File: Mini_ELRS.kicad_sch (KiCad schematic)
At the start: 30 parts, among them J1 Conn_01x02, J2 Conn_01x03_MountingPin, J3 Conn_01x04, J4 Conn_01x03_MountingPin, J5 Conn_01x03_MountingPin, J6 Conn_01x03_MountingPin, Q1 Q_NMOS_GSD, Q2 Q_NMOS_GSD, U1 ESP32-PICO-D4, U2 TC2014-3.3VxCTTR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

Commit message: finished TX mobile
Signed-off-by: huangzzk <huangcmzzk@gmail.com>
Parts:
- removed C3: 180pF, Capacitor_SMD:C_0603_1608Metric, symbol Device:C
- removed J1: Conn_01x02, Connector_PinHeader_2.54mm:PinHeader_2x01_P2.54mm_Vertical, symbol Connector_Generic:Conn_01x02
- removed J2, J4, J5, J6: Conn_01x03_MountingPin, Connector_Molex:Molex_CLIK-Mate_502386-0370_1x03-1MP_P1.25mm_Horizontal, symbol Connector_Generic_MountingPin:Conn_01x03_MountingPin
- removed R2: NC, Resistor_SMD:R_0603_1608Metric, symbol Device:R
- added R7: 10K, Resistor_SMD:R_0603_1608Metric, symbol Device:R
- added TP1: TestPoint, TestPoint:TestPoint_Pad_1.0x1.0mm, symbol Connector:TestPoint
- added U4: CH340E, Package_SO:MSOP-10_3x3mm_P0.5mm, symbol Interface_USB:CH340E
- added USB1: 918-118A2021Y40002, ic_footprint:TYPE-C-SMD_JINGTUOJIN_918-118A2021Y40002, symbol ic:918-118A2021Y40002
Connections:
- net PWM6 is gone; now on net MOSI: U1.36 (IO23)
- net PWM8 is gone; now on net BUSY: U1.42 (IO21)
- net +3V3: now also R7.2, U4.10 (V3), U4.7 (VCC)
- net BUSY: no longer U1.5 (SENSOR_VP)
- net DIO1: now also U1.24 (IO4); no longer U1.7 (SENSOR_CAPN)
- net GND: now also R4.1, U4.3 (GND), USB1.1 (G), USB1.16 (G), USB1.17, USB1.18, USB1.8 (G), USB1.9 (G); no longer R4.2, R6.2
- net LED: now also U1.21 (IO15); no longer U1.22 (IO2)
- net MISO: now also U1.38 (IO19); no longer U1.8 (SENSOR_VN)
- net MOSI: no longer U1.16 (IO27)
- net NRST: now also U1.17 (IO14); no longer U1.24 (IO4)
- net NSS: now also U1.34 (IO5); no longer R6.1, U1.20 (IO13)
- net SCK: now also U1.35 (IO18); no longer U1.18 (IO12)
- net at Q1.3 (D): now also Q2.1 (G), R6.1
- net CRSF: now reaches Q2.3 (D)
- net CRSF: now also U1.20 (IO13), R7.1, U4.9 (RXD)
- net at U1.23 (IO0): now also TP1.1
- net +BATT renamed +5V
- net +5V: now also USB1.10 (V), USB1.15 (V), USB1.2 (V), USB1.7 (V)
- net PWM1: no longer names the net of U1.28 (SD2/IO9)
- net PWM2: no longer names the net of U1.14 (IO25)
- removed net PWM3: Q2.1 (G), R5.1, U1.34 (IO5)
- net PWM4: no longer names the net of U1.13 (IO33)
- removed net PWM5: Q1.1 (G), R4.1, U1.39 (IO22)
- net PWM7: no longer names the net of U1.12 (IO32)
- new net: R5.1, USB1.11 (CC2)
- new net: R4.2, USB1.6 (CC1)
- new net CRSF_TX: Q1.1 (G), U4.8 (TXD)
- new net DN: U4.2 (UD-), USB1.13 (D-), USB1.4 (D-)
- new net DP: U4.1 (UD+), USB1.12 (D+), USB1.5 (D+)
- new net TNOW: R6.2, U4.6 (TNOW)
- no-connect marks 3 -> 4
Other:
- moved on the sheet: C2, C4, U2

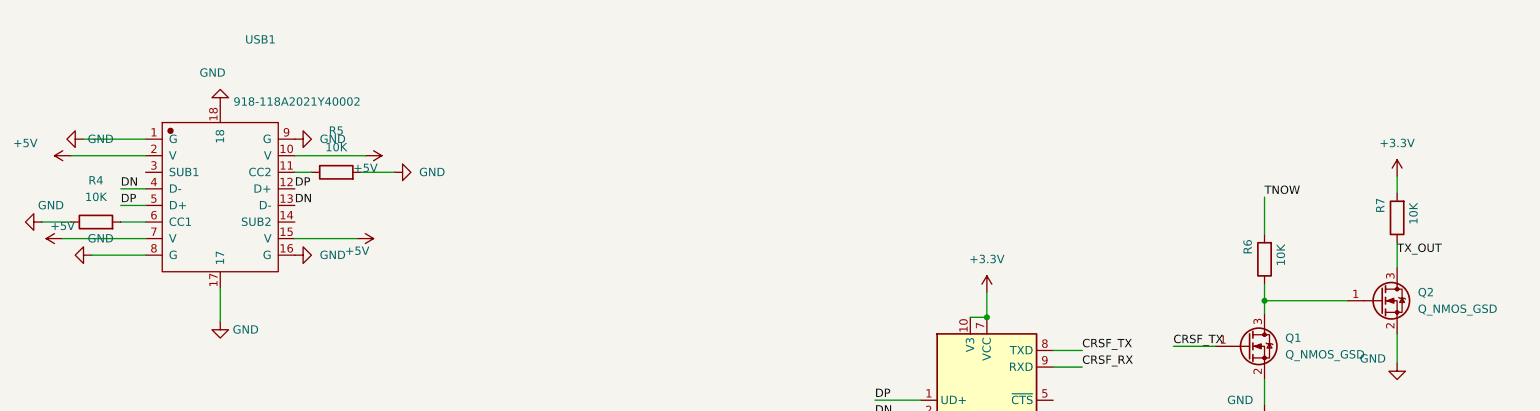
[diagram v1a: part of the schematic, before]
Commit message: change some value of res
Signed-off-by: huangzzk <huangcmzzk@gmail.com>
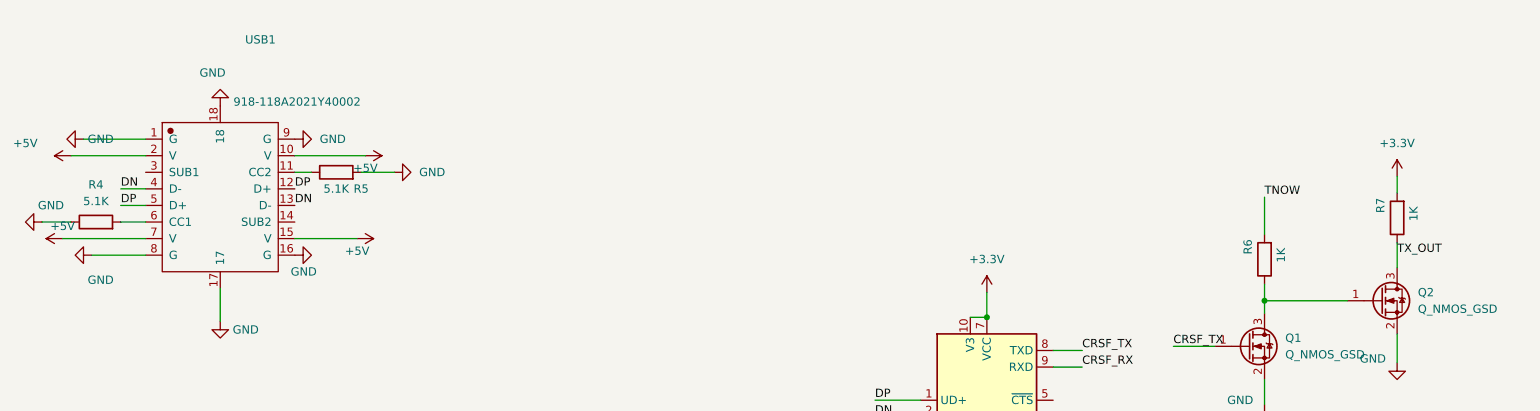
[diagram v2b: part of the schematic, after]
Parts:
- R4, R5: value 10K -> 5.1K
- R6, R7: value 10K -> 1K
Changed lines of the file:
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@@
   )
   (symbol (lib_id "power:GND") (at 72.39 213.995 90) (unit 1)
-    (in_bom yes) (on_board yes) (fields_autoplaced)
+    (in_bom yes) (on_board yes)
     (property "Reference" "#PWR010" (id 0) (at 78.74 213.995 0)
       (effects (font (size 1.27 1.27)) hide)
     )
-    (property "Value" "GND" (id 1) (at 76.2 213.9949 90)
+    (property "Value" "GND" (id 1) (at 71.755 216.535 90)
       (effects (font (size 1.27 1.27)) (justify right))
     )
@@
     (in_bom yes) (on_board yes)
     (property "Reference" "R7" (id 0) (at 238.76 206.375 90))
-    (property "Value" "10K" (id 1) (at 243.84 207.645 90))
+    (property "Value" "1K" (id 1) (at 243.84 207.645 90))
     (property "Footprint" "Resistor_SMD:R_0603_1608Metric" (id 2) (at 243.078 208.28 90)
       (effects (font (size 1.27 1.27)) hide)
@@
   )
   (symbol (lib_id "Device:R") (at 78.74 201.295 90) (unit 1)
-    (in_bom yes) (on_board yes) (fields_autoplaced)
-    (property "Reference" "R5" (id 0) (at 78.74 194.945 90))
-    (property "Value" "10K" (id 1) (at 78.74 197.485 90))
+    (in_bom yes) (on_board yes)
+    (property "Reference" "R5" (id 0) (at 82.55 203.835 90))
+    (property "Value" "5.1K" (id 1) (at 78.74 203.835 90))
     (property "Footprint" "Resistor_SMD:R_0603_1608Metric" (id 2) (at 78.74 203.073 90)
       (effects (font (size 1.27 1.27)) hide)
@@
   (symbol (lib_id "power:+5V") (at 208.28 142.875 0) (unit 1)
     (in_bom yes) (on_board yes) (fields_autoplaced)
-    (property "Reference" "#PWR?" (id 0) (at 208.28 146.685 0)
+    (property "Reference" "#PWR0114" (id 0) (at 208.28 146.685 0)
       (effects (font (size 1.27 1.27)) hide)
     )
@@
   (symbol (lib_id "Device:R") (at 41.91 208.915 90) (unit 1)
     (in_bom yes) (on_board yes) (fields_autoplaced)
-    (property "Reference" "R4" (id 0) (at 41.91 202.565 90))
-    (property "Value" "10K" (id 1) (at 41.91 205.105 90))
+    (property "Reference" "R4" (id 0) (at 41.91 203.2 90))
+    (property "Value" "5.1K" (id 1) (at 41.91 205.74 90))
     (property "Footprint" "Resistor_SMD:R_0603_1608Metric" (id 2) (at 41.91 210.693 90)
       (effects (font (size 1.27 1.27)) hide)
@@
     (in_bom yes) (on_board yes)
     (property "Reference" "R6" (id 0) (at 218.44 212.725 90))
-    (property "Value" "10K" (id 1) (at 223.52 213.995 90))
+    (property "Value" "1K" (id 1) (at 223.52 213.995 90))
     (property "Footprint" "Resistor_SMD:R_0603_1608Metric" (id 2) (at 222.758 214.63 90)
       (effects (font (size 1.27 1.27)) hide)
@@
       (effects (font (size 1.27 1.27)) hide)
     )
-    (property "Value" "GND" (id 1) (at 40.64 211.455 90)
+    (property "Value" "GND" (id 1) (at 40.64 217.805 90)
       (effects (font (size 1.27 1.27)) (justify left))
     )
@@
       (reference "#PWR0113") (unit 1) (value "+3.3V") (footprint "")
     )
+    (path "/6f7ebd79-7887-4082-8403-98a1e65cf572"
+      (reference "#PWR0114") (unit 1) (value "+5V") (footprint "")
+    )
     (path "/c424557c-de60-43fc-9d3b-22dc03bfab6a"
       (reference "#PWR0115") (unit 1) (value "+3.3V") (footprint "")
@@
       (reference "#PWR0122") (unit 1) (value "GND") (footprint "")
     )
-    (path "/6f7ebd79-7887-4082-8403-98a1e65cf572"
-      (reference "#PWR?") (unit 1) (value "+5V") (footprint "")
-    )
     (path "/c8e59e3c-90e9-4055-b7f1-626c5957e4dc"
       (reference "AE1") (unit 1) (value "Antenna") (footprint "RF_Antenna:Johanson_2450AT43F0100")
@@
     )
     (path "/bb8e7ee2-df1a-4e1f-8779-58ad9d62a755"
-      (reference "R4") (unit 1) (value "10K") (footprint "Resistor_SMD:R_0603_1608Metric")
+      (reference "R4") (unit 1) (value "5.1K") (footprint "Resistor_SMD:R_0603_1608Metric")
     )
     (path "/27d6e1a3-3442-40a7-993e-3db446c34a82"
-      (reference "R5") (unit 1) (value "10K") (footprint "Resistor_SMD:R_0603_1608Metric")
+      (reference "R5") (unit 1) (value "5.1K") (footprint "Resistor_SMD:R_0603_1608Metric")
     )
     (path "/bfed96ce-b74a-4237-80ff-a7452d486339"
-      (reference "R6") (unit 1) (value "10K") (footprint "Resistor_SMD:R_0603_1608Metric")
+      (reference "R6") (unit 1) (value "1K") (footprint "Resistor_SMD:R_0603_1608Metric")
     )
     (path "/19fcb816-0635-4db1-b66e-f01e6e080e03"
-      (reference "R7") (unit 1) (value "10K") (footprint "Resistor_SMD:R_0603_1608Metric")
+      (reference "R7") (unit 1) (value "1K") (footprint "Resistor_SMD:R_0603_1608Metric")
     )
     (path "/23d9b4fc-9296-4735-a3b9-4f2cfa199b94"

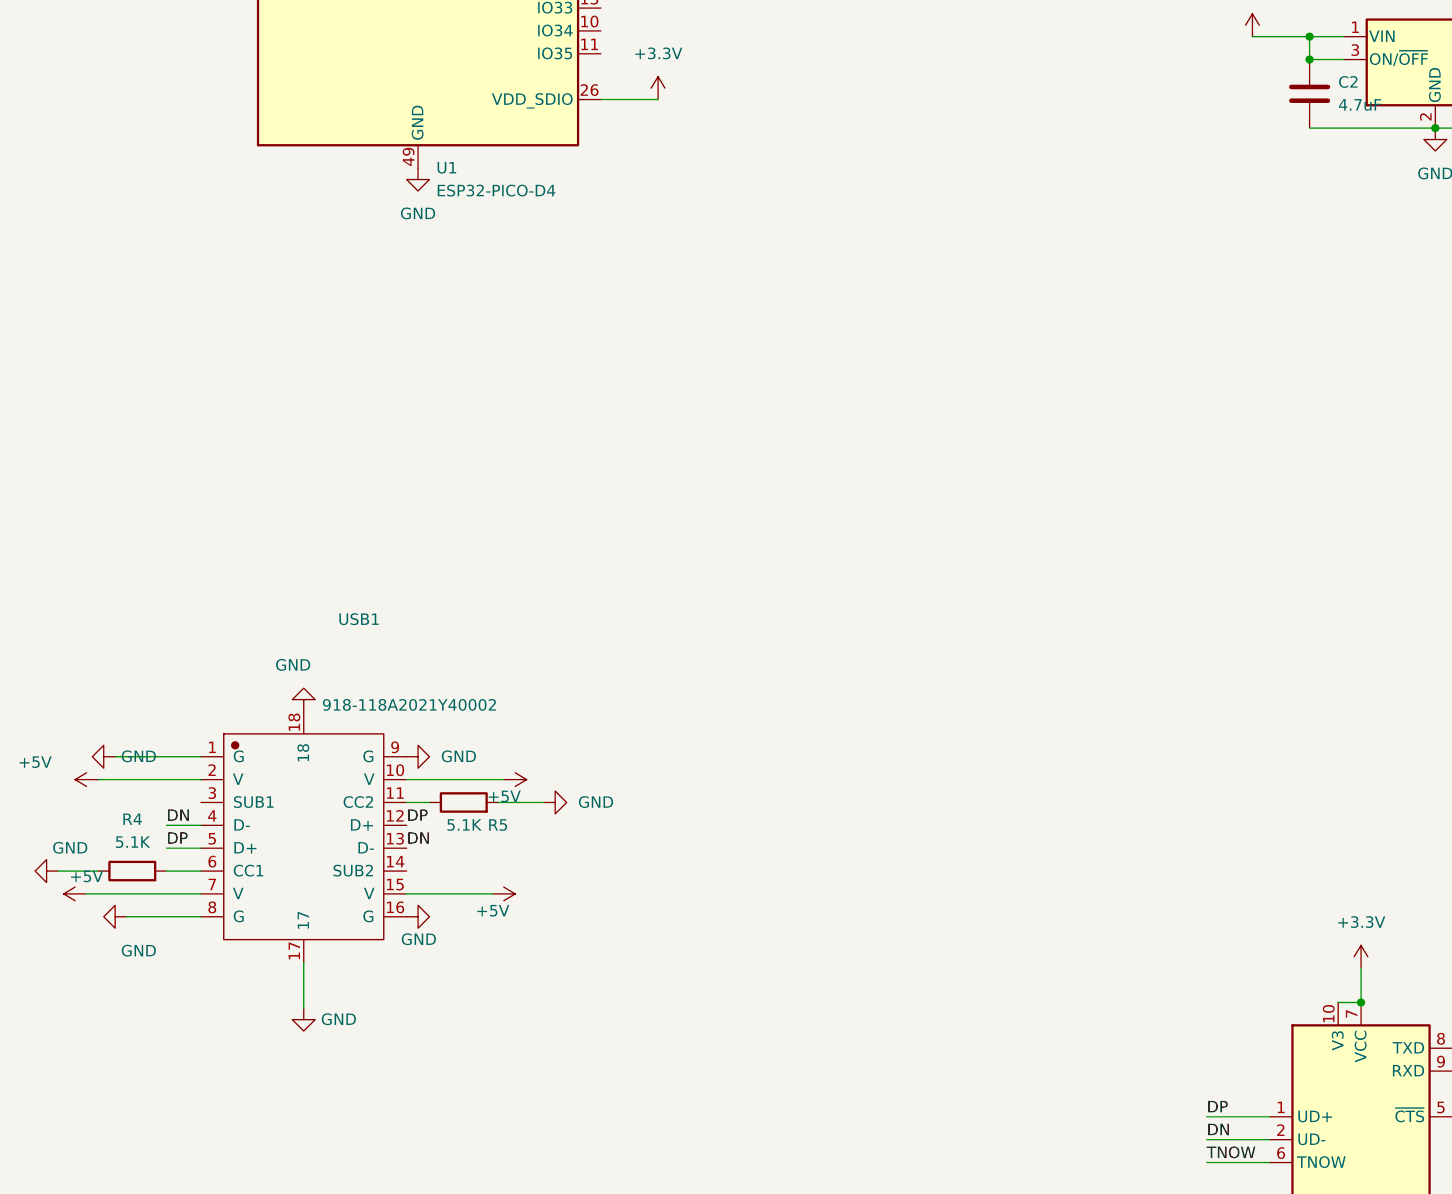
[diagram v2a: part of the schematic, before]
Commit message: use another Type-c package
Signed-off-by: huangzzk <huangcmzzk@gmail.com>
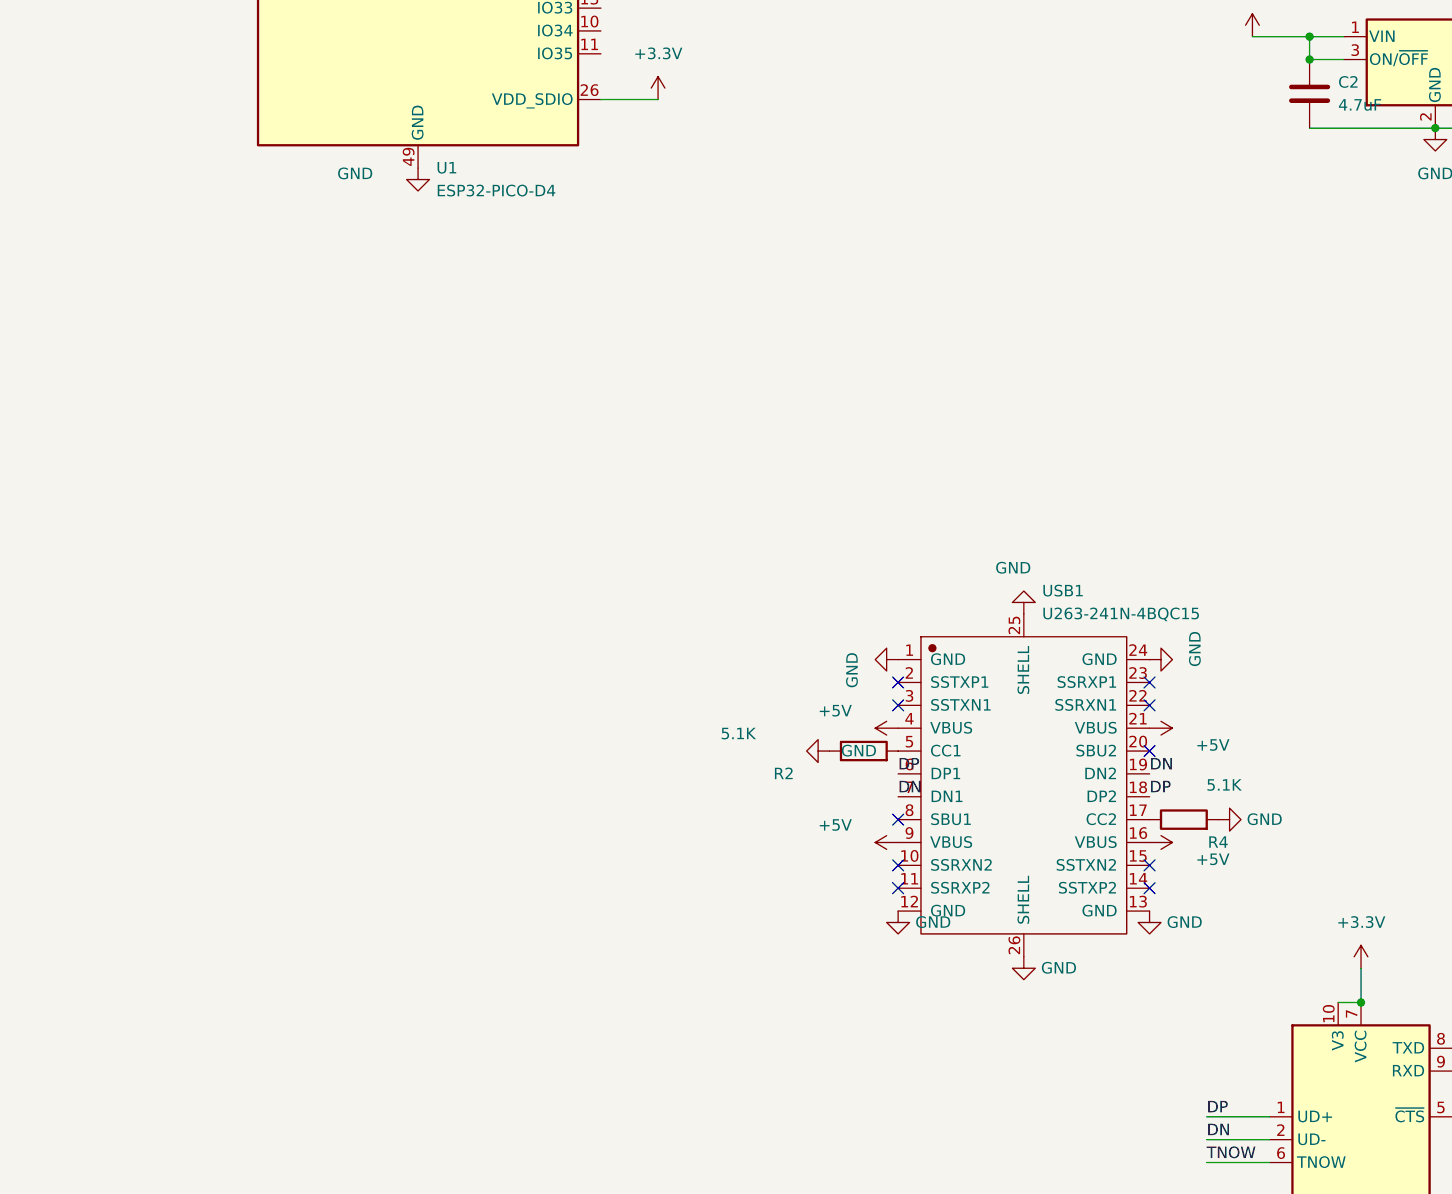
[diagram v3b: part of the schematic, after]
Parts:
- removed R5: 5.1K, Resistor_SMD:R_0603_1608Metric, symbol Device:R
- removed USB1: 918-118A2021Y40002, ic_footprint:TYPE-C-SMD_JINGTUOJIN_918-118A2021Y40002, symbol ic:918-118A2021Y40002
- added R2: 5.1K, Resistor_SMD:R_0603_1608Metric, symbol Device:R
- added USB1: U263-241N-4BQC15, ic_footprint:USB-C-SMD_U263-241N-4BQC15, symbol ic:U263-241N-4BQC15
- TP1: footprint TestPoint:TestPoint_Pad_1.0x1.0mm -> TestPoint:TestPoint_THTPad_1.0x1.0mm_Drill0.5mm
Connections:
- net +5V: now also USB1.16 (VBUS), USB1.21 (VBUS), USB1.4 (VBUS), USB1.9 (VBUS)
- net DN: now also USB1.19 (DN2), USB1.7 (DN1)
- net DP: now also USB1.18 (DP2), USB1.6 (DP1)
- net GND: now also R4.2, R2.1, USB1.1 (GND), USB1.12 (GND), USB1.13 (GND), USB1.24 (GND), USB1.25 (SHELL), USB1.26 (SHELL); no longer R4.1
- new net: R4.1, USB1.17 (CC2)
- new net: R2.2, USB1.5 (CC1)
- no-connect marks 4 -> 14
